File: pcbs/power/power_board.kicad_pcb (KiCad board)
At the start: 2 copper layers, 114 x 137.6 mm, 37 parts, among them J1 PinSocket_1x04_P2.54, J10 MR30PW-M, J11 MR30PW-M, J12 12V connection, J2 PinSocket_1x04_P2.54, J3 PinSocket_1x04_P2.54, J4 JST_XH_B3B, J5 JST_XH_B3B, J6 XT30PW-F, J7 XT30PW-F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

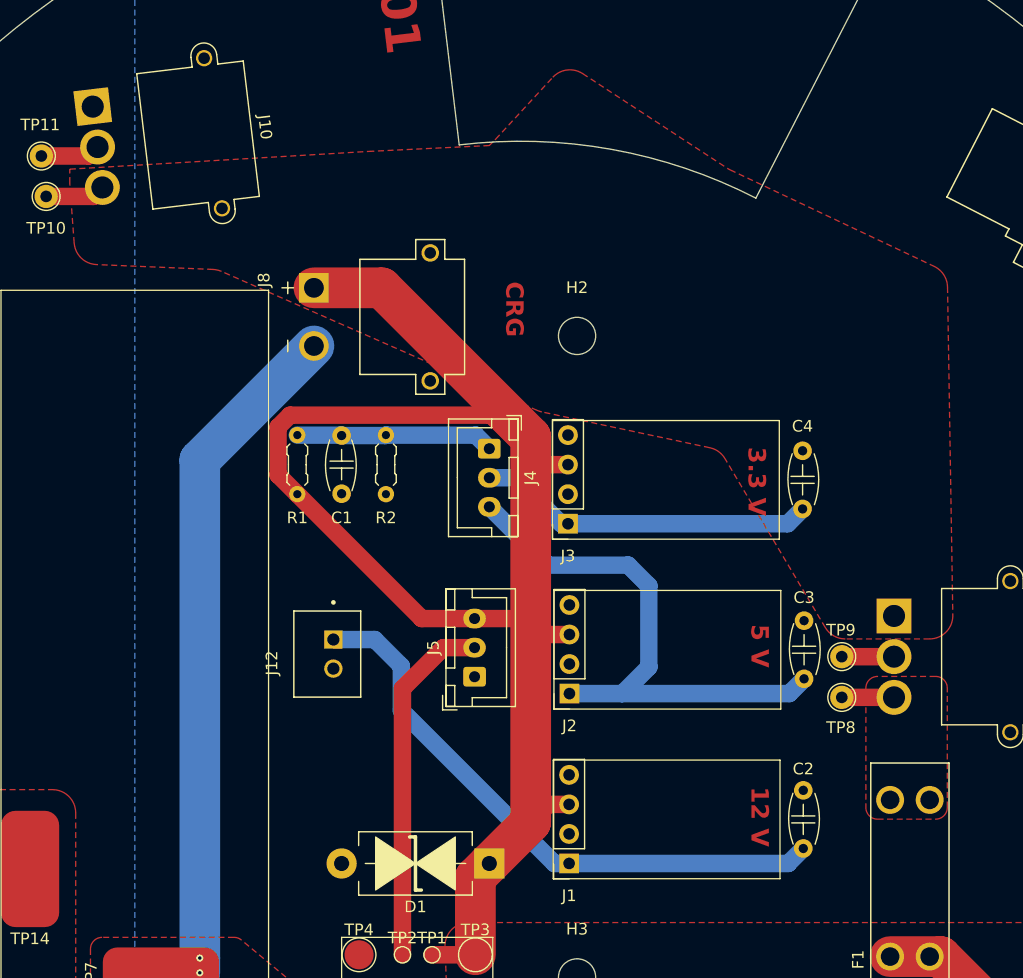
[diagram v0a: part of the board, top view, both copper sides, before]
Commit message: Updated Power-Board PCB design
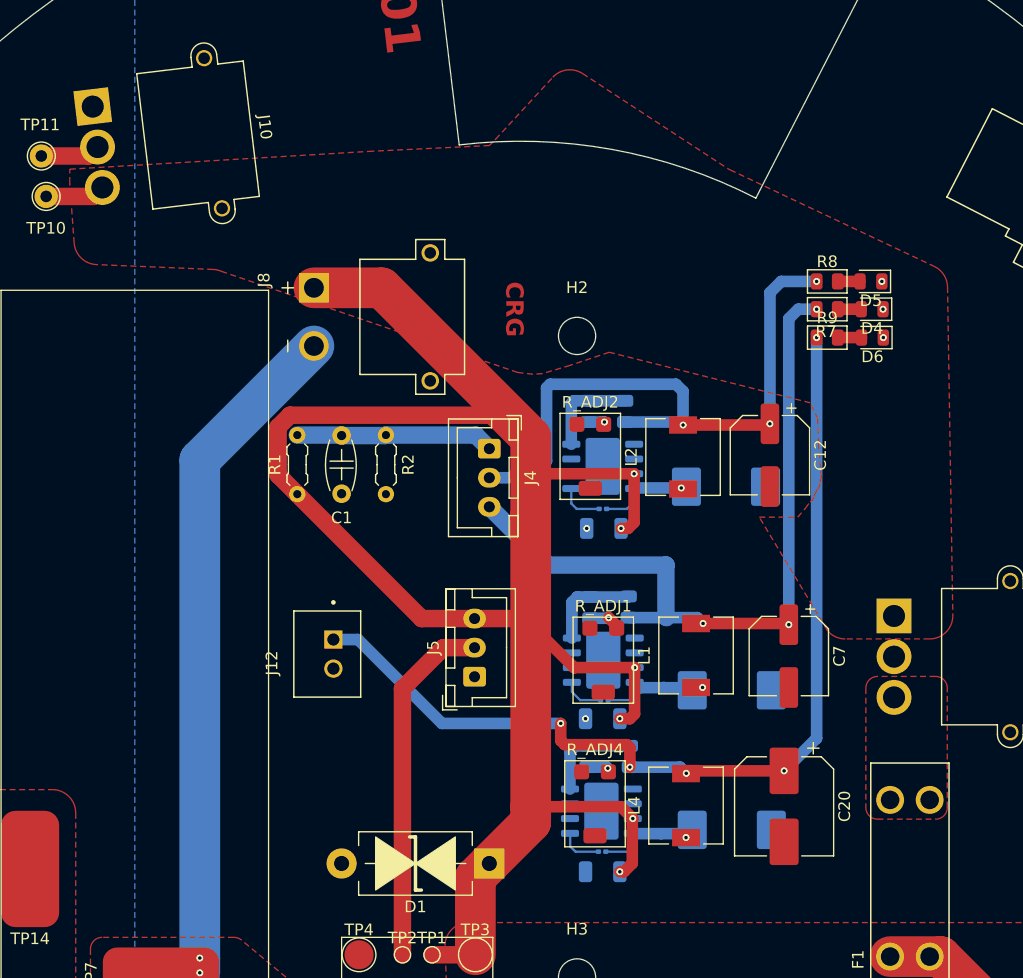
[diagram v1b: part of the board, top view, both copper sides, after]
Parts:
- removed J1, J2, J3: PinSocket_1x04_P2.54, Connector_PinSocket_2.54mm:PinSocket_1x04_P2.54mm_Vertical
- removed TP8: B6, TestPoint:TestPoint_THTPad_D2.0mm_Drill1.0mm
- removed TP9: B5, TestPoint:TestPoint_THTPad_D2.0mm_Drill1.0mm
- added C12: 220uF, Capacitor_SMD:CP_Elec_6.3x7.7, F.Cu at (110.4, 86.8)
- added C20: 220uF, Capacitor_SMD:CP_Elec_8x6.2, F.Cu at (111.6, 117.0)
- added C5: 0.01uF, Capacitor_SMD:C_0201_0603Metric, B.Cu at (96.0, 120.9)
- added C6: 0.01uF, Capacitor_SMD:C_0201_0603Metric, B.Cu at (96.2, 107.8)
- added C7: 220uF, Capacitor_SMD:CP_Elec_6.3x7.7, F.Cu at (112.1, 104.0)
- added C8: 10uF, Capacitor_SMD:C_1206_3216Metric, B.Cu at (96.1, 109.4)
- added D2: B340, Diode_SMD:D_SMC, B.Cu at (106.7, 89.5)
- added D3: B340, Diode_SMD:D_SMC, B.Cu at (107.2, 119.0)
- added D4: LED, LED_SMD:LED_0805_2012Metric, F.Cu at (119.2, 74.2)
- added D5: LED, LED_SMD:LED_0805_2012Metric, F.Cu at (119.1, 71.8)
- added D6: LED, LED_SMD:LED_0805_2012Metric, F.Cu at (119.2, 76.7)
- added D7: B340, Diode_SMD:D_SMC, B.Cu at (107.2, 107.0)
- added L1: 22uH, Inductor_SMD:L_6.3x6.3_H3, F.Cu at (104.1, 104.0)
- added L2: 22uH, Inductor_SMD:L_6.3x6.3_H3, F.Cu at (103.0, 86.9)
- added L4: 22uH, Inductor_SMD:L_6.3x6.3_H3, F.Cu at (103.2, 116.9)
- added R15: 1k, PCM_Resistor_SMD_AKL:R_0805_2012Metric, B.Cu at (94.7, 112.7)
- added R16: 10k, PCM_Resistor_SMD_AKL:R_0805_2012Metric, B.Cu at (98.4, 112.7)
- added R3: 10k, PCM_Resistor_SMD_AKL:R_0805_2012Metric, B.Cu at (98.3, 99.8)
- added R4: 2.7k, PCM_Resistor_SMD_AKL:R_0805_2012Metric, B.Cu at (95.0, 99.9)
- added R5: 5.6k, PCM_Resistor_SMD_AKL:R_0805_2012Metric, B.Cu at (94.8, 83.0)
- added R6: 10k, PCM_Resistor_SMD_AKL:R_0805_2012Metric, B.Cu at (98.0, 83.0)
- added R7: 330, PCM_Resistor_SMD_AKL:R_0805_2012Metric, F.Cu at (115.4, 74.2)
- added R8: 120, PCM_Resistor_SMD_AKL:R_0805_2012Metric, F.Cu at (115.4, 71.8)
- added R9: 1k, PCM_Resistor_SMD_AKL:R_0805_2012Metric, F.Cu at (115.4, 76.7)
- added R_ADJ1: 1k, PCM_Potentiometer_SMD_AKL:Potentiometer_Bourns_3314G_Vertical, F.Cu at (96.1, 104.4)
- added R_ADJ2: 1k, PCM_Potentiometer_SMD_AKL:Potentiometer_Bourns_3314G_Vertical, F.Cu at (95.0, 86.9)
- added R_ADJ4: 220, PCM_Potentiometer_SMD_AKL:Potentiometer_Bourns_3314G_Vertical, F.Cu at (95.4, 116.7)
- added U1: TPS5430DDA, PCM_Package_SO_AKL:Texas_HSOP-8-1EP_3.9x4.9mm_P1.27mm, B.Cu at (96.1, 104.4)
- added U2: TPS5430DDA, PCM_Package_SO_AKL:Texas_HSOP-8-1EP_3.9x4.9mm_P1.27mm, B.Cu at (96.1, 87.7)
- added U4: TPS5430DDA, PCM_Package_SO_AKL:Texas_HSOP-8-1EP_3.9x4.9mm_P1.27mm, B.Cu at (95.9, 117.4)
- C2, C3: value 100nF -> 10uF; footprint PCM_Capacitor_THT_AKL:C_Disc_D5.0mm_W2.5mm_P5.00mm -> Capacitor_SMD:C_1206_3216Metric; moved to B.Cu
- C4: value 100nF -> 0.01uF; footprint PCM_Capacitor_THT_AKL:C_Disc_D5.0mm_W2.5mm_P5.00mm -> Capacitor_SMD:C_0201_0603Metric; moved to B.Cu
- moved C2 28.3 mm to (96.2, 93.1), turned to 0 degrees
- moved C3 27.7 mm to (96.1, 122.6), turned to 0 degrees
- moved C4 17.9 mm to (96.1, 91.4), turned to 180 degrees
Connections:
- C2 pad 2: +12V -> V_{ BATT}
- C3 pad 2: +5V -> V_{ BATT}
- C4 pad 1: GND -> Net-(D2-K)
- C4 pad 2: +3.3V -> Net-(U2-BOOT)
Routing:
- net V_{ BATT}: track 223.6 -> 260.0 mm, vias 0 -> 6
- net +12V: track 51.1 -> 83.9 mm, vias 0 -> 5
- net +3.3V: track 29.1 -> 55.1 mm, vias 0 -> 3
- net +5V: track 47.4 -> 64.9 mm, vias 0 -> 3
- net Net-(D7-K): track 0.00 -> 9.75 mm, vias 0 -> 1
- net Net-(U4-VSENSE): track 0.00 -> 8.58 mm
- net Net-(D3-K): track 0.00 -> 8.38 mm, vias 0 -> 1
- net Net-(U2-VSENSE): track 0.00 -> 8.24 mm
- net Net-(U1-VSENSE): track 0.00 -> 8.16 mm
- net Net-(D2-K): track 0.00 -> 7.83 mm, vias 0 -> 1
- net Net-(J9-Pin_2): track 4.49 -> 0.00 mm
- net /B_{6s}: track 4.49 -> 0.00 mm
- net Net-(U2-BOOT): track 0.00 -> 3.88 mm
- net Net-(U4-BOOT): track 0.00 -> 3.74 mm
- net Net-(U1-BOOT): track 0.00 -> 3.58 mm
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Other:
- board text removed: "12 V"
- board text removed: "3.3 V"
- board text removed: "5 V"
